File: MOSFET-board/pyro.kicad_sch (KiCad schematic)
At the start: 11 parts, among them U1 BTS3080EJXUMA1, U24 ADA4897-1ARJZ-R7

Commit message: Progress on revising ground boards.
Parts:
- removed D43: D_Schottky, Diode_SMD:D_0603_1608Metric, symbol Device:D_Schottky
- removed D9: G_LED, LED_SMD:LED_0603_1608Metric, symbol Device:LED_Small
- removed R10, R93: 10k, Resistor_SMD:R_0603_1608Metric, symbol Device:R_Small
- removed R103: 2k, Resistor_SMD:R_0603_1608Metric, symbol Device:R_Small
- removed R73: 1k, Resistor_SMD:R_0603_1608Metric, symbol Device:R_Small
- removed R83: 9k, Resistor_SMD:R_0603_1608Metric, symbol Device:R_Small
- removed R9: 100, Resistor_SMD:R_0603_1608Metric, symbol Device:R_Small
- removed U1: BTS3080EJXUMA1, BTS3080EJXUMA1:SOIC127P600X115-9N, symbol BTS3080EJXUMA1:BTS3080EJXUMA1
- removed U24: ADA4897-1ARJZ-R7, Symbol:SOT95P280X145-6N, symbol Amplifier_Operational:ADA4897-1ARJZ-R7
- added D18: D_Schottky, Diode_SMD:D_0603_1608Metric, symbol Device:D_Schottky
- added D4: G_LED, LED_SMD:LED_0603_1608Metric, symbol Device:LED_Small
- added Q13: Q_PMOS_GDS, symbol Device:Q_PMOS_GDS
- added R27: 10k, Resistor_SMD:R_0603_1608Metric, symbol Device:R_Small
- added R43: 470, Resistor_SMD:R_0603_1608Metric, symbol Device:R_Small
- added R7: 1k, Resistor_SMD:R_0603_1608Metric, symbol Device:R_Small
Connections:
- net +5V: now also Q13.2 (D), R27.1
- net In: now also R7.1
- net Out: now also F4.1; no longer F4.2
- new net: D4.2 (A), R43.1
- new net: D18.1 (K), F4.2, Q13.3 (S), R43.2
- new net: Q13.1 (G), R27.2, R7.2
- new net -7 V: D18.2 (A), D4.1 (K)
- no-connect marks 2 -> 0
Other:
- note removed: "STATUS should be connected to an external pull-up resistor. When IC shutdown (eg: thermal runaway), it activate internal pull-down resistor. This will drive 3V3 across the LED."

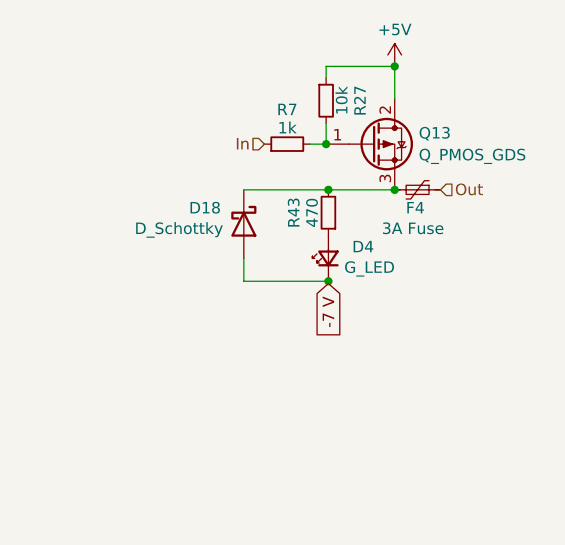
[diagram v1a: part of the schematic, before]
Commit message: Further revision. Two batteries system.
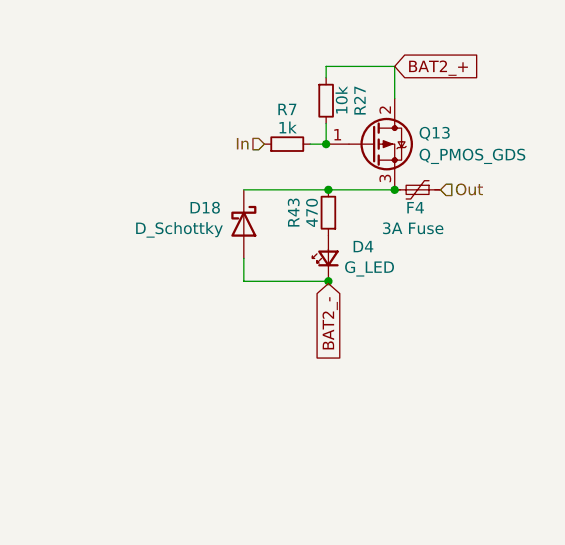
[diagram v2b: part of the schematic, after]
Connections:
- net +5V renamed BAT2_+
- net -7 V renamed BAT2_-
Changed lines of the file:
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@@
   (junction (at 82.55 56.896) (diameter 0) (color 0 0 0 0)
   )
-  (junction (at 89.916 43.18) (diameter 0) (color 0 0 0 0)
-  )
   (junction (at 82.296 51.816) (diameter 0) (color 0 0 0 0)
   )
@@
     (stroke (width 0) (type default))
   )
-  (global_label "-7 V" (shape input) (at 82.55 67.31 270) (fields_autoplaced)
+  (global_label "BAT2_+" (shape input) (at 89.916 43.18 0) (fields_autoplaced)
+    (effects (font (size 1.27 1.27)) (justify left))
+    (property "Intersheetrefs" "${INTERSHEET_REFS}" (at 99.9769 43.18 0)
+      (effects (font (size 1.27 1.27)) (justify left) hide)
+    )
+  )
+  (global_label "BAT2_-" (shape input) (at 82.55 67.31 270) (fields_autoplaced)
     (effects (font (size 1.27 1.27)) (justify right))
-    (property "Intersheetrefs" "${INTERSHEET_REFS}" (at 82.55 75.1333 90)
+    (property "Intersheetrefs" "${INTERSHEET_REFS}" (at 82.55 77.3709 90)
       (effects (font (size 1.27 1.27)) (justify right) hide)
     )
@@
         )
       )
-    )
-  )
-  (symbol (lib_id "power:+5V") (at 89.916 43.18 0) (unit 1)
-    (in_bom yes) (on_board yes) (dnp no) (fields_autoplaced)
-    (property "Reference" "#PWR069" (at 89.916 46.99 0)
-      (effects (font (size 1.27 1.27)) hide)
-    )
-    (property "Value" "+5V" (at 89.916 39.116 0)
-      (effects (font (size 1.27 1.27)))
-    )
-    (property "Footprint" "" (at 89.916 43.18 0)
-      (effects (font (size 1.27 1.27)) hide)
-    )
-    (property "Datasheet" "" (at 89.916 43.18 0)
-      (effects (font (size 1.27 1.27)) hide)
-    )
-    (pin "1")
-    (instances
-      (project "MOSFET-board"
-        (path "/eeff6235-4c56-4b47-a90f-883101560994/893d1dd2-3918-4c33-bb19-565952861d30"
-          (reference "#PWR069") (unit 1)
-        )
-        (path "/eeff6235-4c56-4b47-a90f-883101560994/ed8a8d2e-acc7-4ab1-ad3e-27a6738380d1"
-          (reference "#PWR067") (unit 1)
-        )
-        (path "/eeff6235-4c56-4b47-a90f-883101560994/24e6f781-7c8b-4994-87df-00244dd6f39a"
-          (reference "#PWR068") (unit 1)
-        )
-        (path "/eeff6235-4c56-4b47-a90f-883101560994/91bdbe40-1bb3-4c62-9e5c-60fa44689352"
-          (reference "#PWR070") (unit 1)
-        )
-        (path "/eeff6235-4c56-4b47-a90f-883101560994/cd0c8342-bbee-4b11-b720-e7d030d8c579"
-          (reference "#PWR071") (unit 1)
-        )
-        (path "/eeff6235-4c56-4b47-a90f-883101560994/b7c464b0-d133-4d7c-85db-a1e6fa29541a"
-          (reference "#PWR072") (unit 1)
-        )
-        (path "/eeff6235-4c56-4b47-a90f-883101560994/f50c45b0-5df9-4e33-b685-87d9ca9631b8"
-          (reference "#PWR073") (unit 1)
-        )
-        (path "/eeff6235-4c56-4b47-a90f-883101560994/17e1af1c-892c-44b5-9f21-13c67f8345c1"
-          (reference "#PWR074") (unit 1)
-        )
-        (path "/eeff6235-4c56-4b47-a90f-883101560994/9834d00b-56eb-4364-ac20-1e65e4de6ea7"
-          (reference "#PWR075") (unit 1)
-        )
-        (path "/eeff6235-4c56-4b47-a90f-883101560994/828e94c7-3d68-4f8b-8067-489ddf2104fa"
-          (reference "#PWR076") (unit 1)
-        )
-      )
